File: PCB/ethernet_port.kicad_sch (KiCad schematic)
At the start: 53 parts, among them IC10 MMBT3904-AQ, IC11 MMBT3904-AQ, IC5 W5500, IC6 CP2102N-A02-GQFN24, IC7 USBLC6-2SC6, J1 USB_C_Receptacle_USB2.0_16P, J2 TMJ0026ABNL, Y3 ASE-25.000MHZ-LC-T

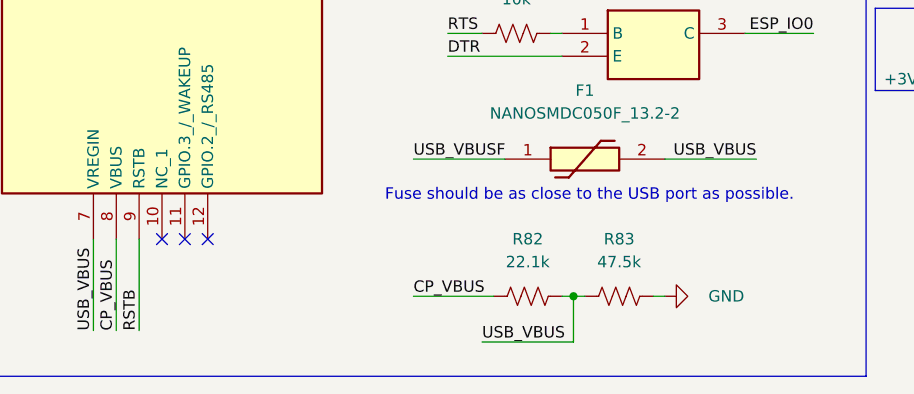
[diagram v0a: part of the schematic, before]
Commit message: Add bottom hand-solder caps and update BOM
Update PCB to add bottom-side hand-solder 0805 capacitor footprints and sync BOM. DarkMagic.csv: increment 0.1uF part count (34→35) and 4.7uF count (1→2) and update component lists. DarkMagic.kicad_pcb: add two B.Cu hand-solder capacitor footprints (C7, C10), adjust several footprint attributes (mark many SMD/TH pads as DNP or set solder_mask_margin), tweak some pad/part positions and UUIDs, and rename one net from /USB_VBUS to /CP_VBUS. Also add generated files (PCB/bom/ibom.html and PCB/database/project.db) and other production file updates to keep project metadata in sync.
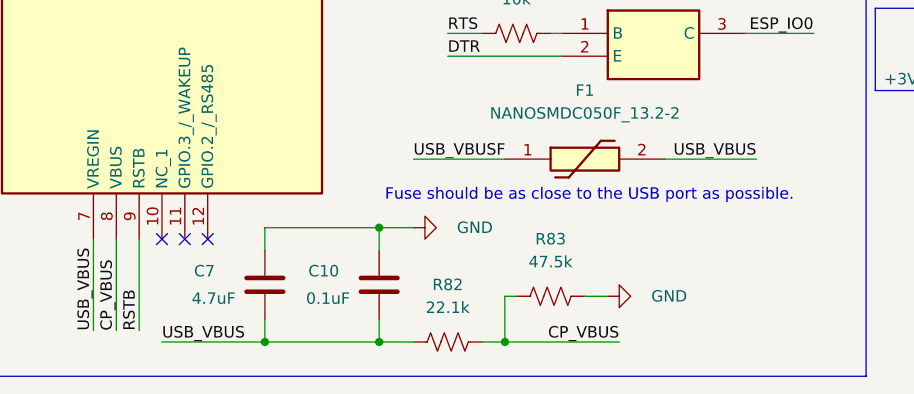
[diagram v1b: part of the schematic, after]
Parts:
- added C10: 0.1uF, Capacitor_SMD:C_0805_2012Metric_Pad1.18x1.45mm_HandSolder, symbol Device:C
- added C7: 4.7uF, Capacitor_SMD:C_0805_2012Metric_Pad1.18x1.45mm_HandSolder, symbol Device:C
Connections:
- net CP_VBUS: now also R83.1
- net GND: now also C10.2, C7.2
- net USB_VBUS: now also C10.1, C7.1; no longer R83.1
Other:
- moved on the sheet: R82, R83

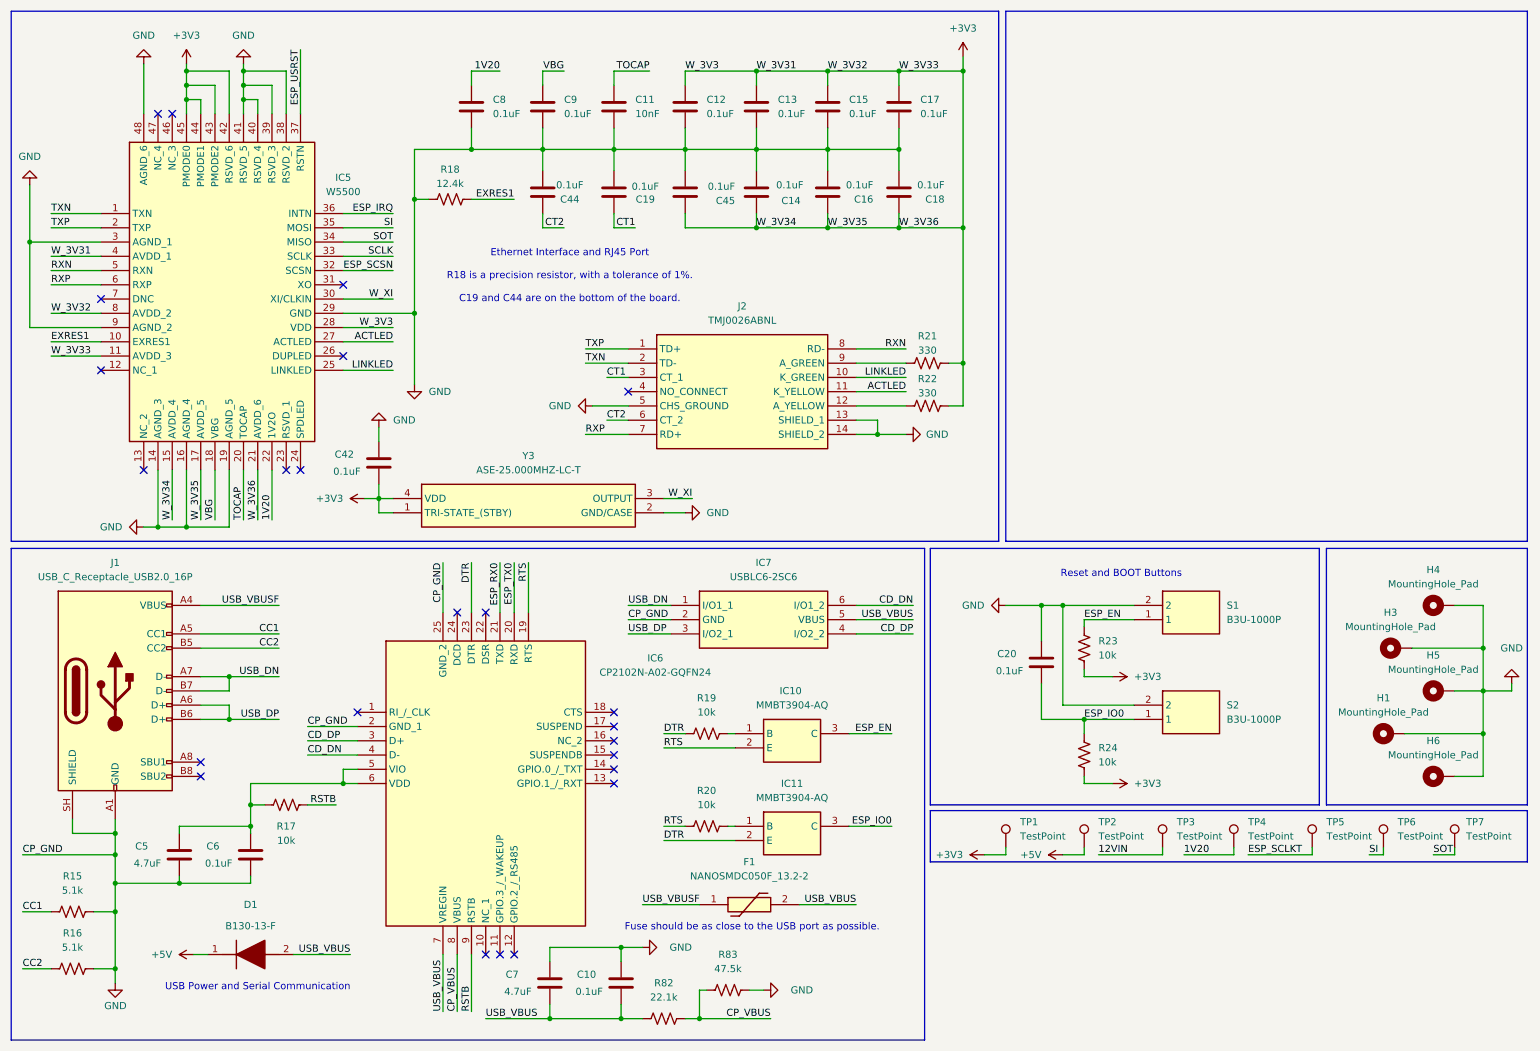
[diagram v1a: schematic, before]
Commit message: Add four 49.9Ω resistors and update PCB
Add R89–R92 as 49.9Ω SMD 0805 hand-solder footprints and corresponding BOM entries. Update PCB layout with new footprints, vias and copper segments to connect the parts into +3V3 and related signal nets (RX/TX pairs), adjust silk/fab properties, and tweak trace geometry. Update production files (BOM, designators, positions, netlist, production archive) and ethernet_port schematic to reflect the changes; add KiCad schematic lock file.
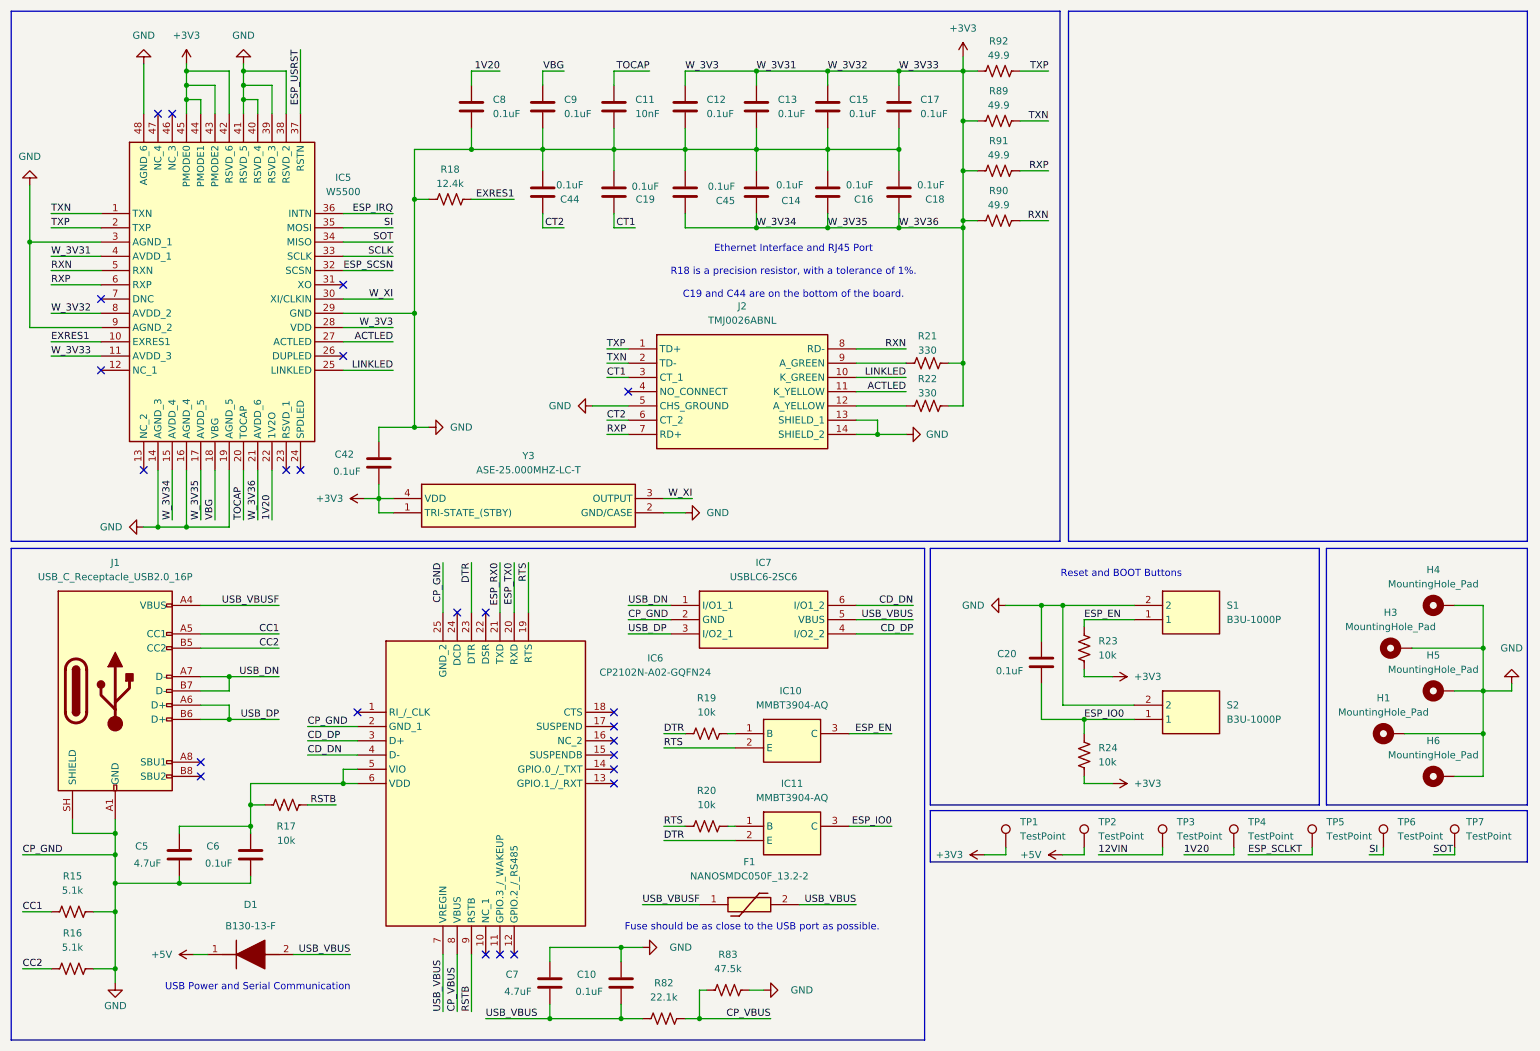
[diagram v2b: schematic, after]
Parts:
- added R89, R90, R91, R92: 49.9, Resistor_SMD:R_0805_2012Metric_Pad1.20x1.40mm_HandSolder, symbol Device:R_US
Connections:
- net +3V3: now also R89.1, R90.1, R91.1, R92.1
- net RXN: now also R90.2
- net RXP: now also R91.2
- net TXN: now also R89.2
- net TXP: now also R92.2

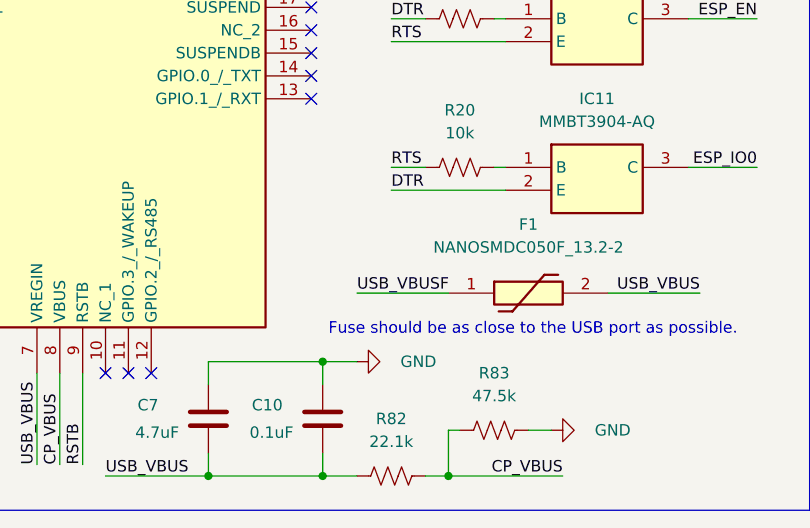
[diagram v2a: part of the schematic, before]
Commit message: PCB: Reroute nets and update component value
Modify DarkMagic.kicad_pcb to correct power routing and update a component value. Changes include: changed a component Value from "CDCLVC1106PWR" to "5PB1106PGGI8", reassigned a pad/net from GND to +3V3, moved a via, removed and added several F.Cu segments (cleaned up GND segments and added +3V3 traces), and adjusted a board polygon/outline coordinate. These edits fix net connections and reflect the correct part designation in the PCB layout.
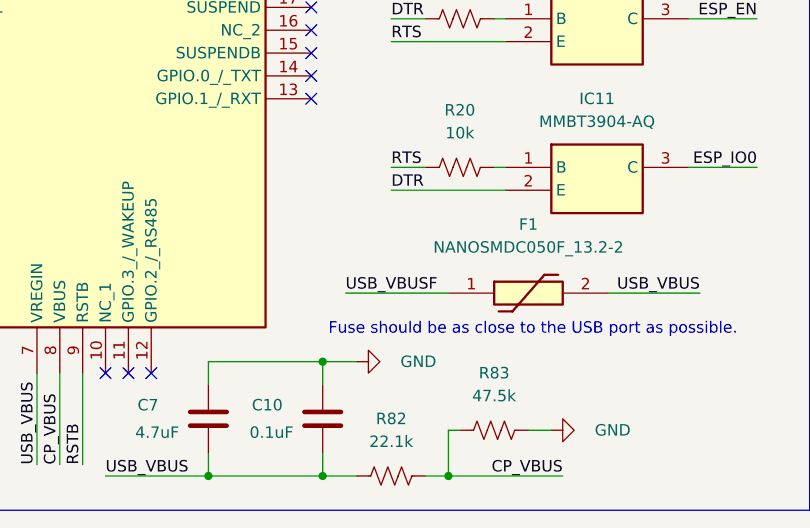
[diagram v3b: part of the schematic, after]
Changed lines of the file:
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@@
 	(wire
 		(pts
-			(xy 125.73 172.72) (xy 135.89 172.72)
+			(xy 124.46 172.72) (xy 135.89 172.72)
 		)
 		(stroke
@@
 	)
 	(label "USB_VBUSF"
-		(at 125.73 172.72 0)
-		(effects
-			(font
+		(at 124.46 172.72 0)
+		(effects
+			(font

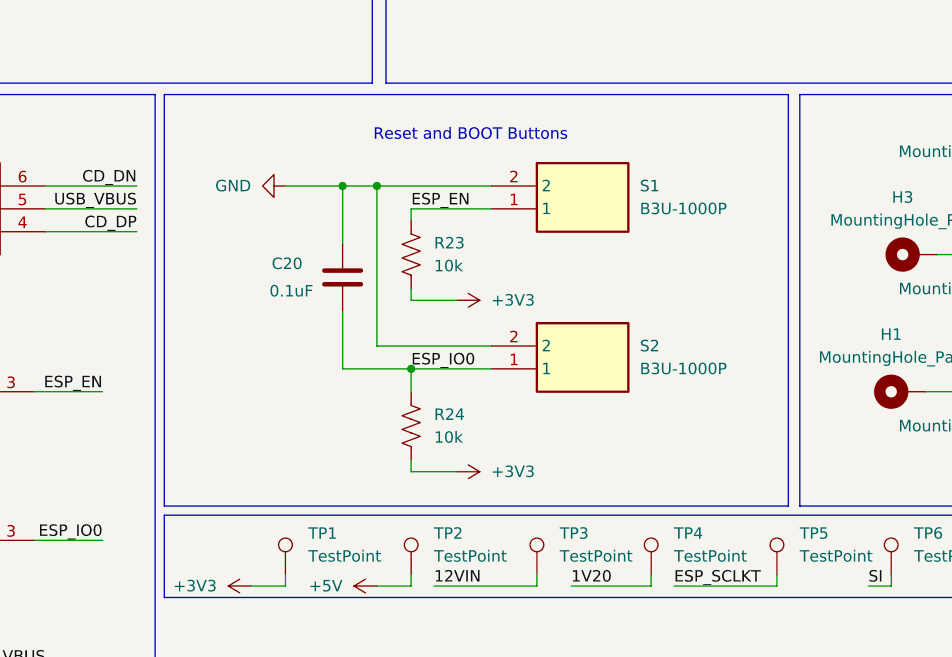
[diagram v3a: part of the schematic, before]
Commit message: V2 Polishing
Minor layout optimizations, including removed vias and rerouted power rails
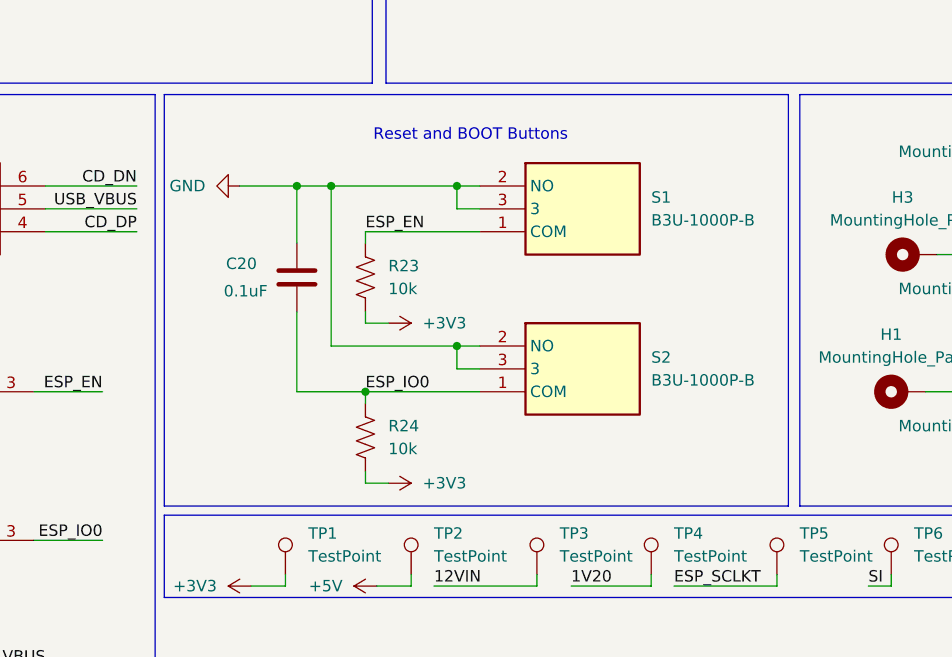
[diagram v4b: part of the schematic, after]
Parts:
- removed S1, S2: B3U-1000P, DarkMagic:B3U-1000P, symbol B3U-1000P:B3U-1000P
- added S1: B3U-1000P-B, DarkMagic:B3U1000PB, symbol B3U-1000P-B:B3U-1000P-B
- added S2: B3U-1000P-B, B3U1000PB, symbol B3U-1000P-B:B3U-1000P-B
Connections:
- net ESP_EN: now also S1.1 (COM)
- net ESP_IO0: now also S2.1 (COM)
- net GND: now also S1.2 (NO), S1.3, S2.2 (NO), S2.3
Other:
- moved on the sheet: C20, R23, R24

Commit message: feat: initialize project with ESP32 schematic, ethernet port layout, and base firmware.
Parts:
- added TP8: TestPoint, TestPoint:TestPoint_Pad_D3.0mm, symbol Connector:TestPoint
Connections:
- net USB_VBUS: now also TP8.1
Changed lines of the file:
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@@
 	(text "USB Power and Serial Communication"
 		(exclude_from_sim no)
-		(at 57.15 187.452 0)
+		(at 57.15 193.294 0)
 		(effects
 			(font
@@
 		(color 0 0 0 0)
 	)
+	(junction
+		(at 66.04 181.61)
+		(diameter 0)
+		(color 0 0 0 0)
+	)
 	(no_connect
 		(at 120.65 148.59)
@@
 	(wire
 		(pts
+			(xy 69.85 186.69) (xy 66.04 186.69)
+		)
+		(stroke
+			(width 0)
+			(type default)
+		)
+	)
+	(wire
+		(pts
 			(xy 158.75 49.53) (xy 158.75 52.07)
 		)
@@
 	(wire
 		(pts
+			(xy 66.04 181.61) (xy 78.74 181.61)
+		)
+		(stroke
+			(width 0)
+			(type default)
+		)
+	)
+	(wire
+		(pts
 			(xy 78.74 87.63) (xy 78.74 90.17)
 		)
@@
 	(wire
 		(pts
-			(xy 63.5 181.61) (xy 73.66 181.61)
+			(xy 63.5 181.61) (xy 66.04 181.61)
 		)
 		(stroke
@@
 	(wire
 		(pts
+			(xy 66.04 186.69) (xy 66.04 181.61)
+		)
+		(stroke
+			(width 0)
+			(type default)
+		)
+	)
+	(wire
+		(pts
 			(xy 146.05 24.13) (xy 146.05 26.67)
 		)
@@
 	)
 	(label "USB_VBUS"
-		(at 73.66 181.61 180)
+		(at 78.74 181.61 180)
 		(effects
 			(font
@@
 					(unit 1)
 				)
+			)
+		)
+	)
+	(symbol
+		(lib_id "Connector:TestPoint")
+		(at 69.85 186.69 270)
+		(unit 1)
+		(body_style 1)
+		(exclude_from_sim no)
+		(in_bom no)
+		(on_board yes)
+		(in_pos_files yes)
+		(dnp no)
+		(fields_autoplaced yes)
+		(property "Reference" "TP8"
+			(at 74.93 185.4199 90)
+			(show_name no)
+			(do_not_autoplace no)
+			(effects
+				(font
+					(size 1.27 1.27)
+				)
+				(justify left)
+			)
+		)
+		(property "Value" "TestPoint"
+			(at 74.93 187.9599 90)
+			(show_name no)
+			(do_not_autoplace no)
+			(effects
+				(font
+					(size 1.27 1.27)
+				)
+				(justify left)
+			)
+		)
+		(property "Footprint" "TestPoint:TestPoint_Pad_D3.0mm"
+			(at 69.85 191.77 0)
+			(hide yes)
+			(show_name no)
+			(do_not_autoplace no)
+			(effects
+				(font
+					(size 1.27 1.27)
+				)
+			)
+		)
+		(property "Datasheet" ""
+			(at 69.85 191.77 0)
+			(hide yes)
+			(show_name no)
+			(do_not_autoplace no)
+			(effects
+				(font
+					(size 1.27 1.27)
+				)
+			)
+		)
+		(property "Description" "test point"
+			(at 69.85 186.69 0)
+			(hide yes)
+			(show_name no)
+			(do_not_autoplace no)
+			(effects
+				(font
+					(size 1.27 1.27)
+				)
+			)
+		)
+		(property "Maunfacturer Part Number" ""
+			(at 69.85 186.69 0)
+			(hide yes)
+			(show_name no)
+			(do_not_autoplace no)
+			(effects
+				(font
+					(size 1.27 1.27)
+				)
+			)
+		)
+		(property "AVAILABILITY" ""
+			(at 69.85 186.69 0)
+			(hide yes)
+			(show_name no)
+			(do_not_autoplace no)
+			(effects
+				(font
+					(size 1.27 1.27)
+				)
+			)
+		)
+		(property "Check_prices" ""
+			(at 69.85 186.69 0)
+			(hide yes)
+			(show_name no)
+			(do_not_autoplace no)
+			(effects
+				(font
+					(size 1.27 1.27)
+				)
+			)
+		)
+		(property "MF" ""
+			(at 69.85 186.69 0)
+			(hide yes)
+			(show_name no)
+			(do_not_autoplace no)
+			(effects
+				(font
+					(size 1.27 1.27)
+				)
+			)
+		)
+		(property "MP" ""
+			(at 69.85 186.69 0)
+			(hide yes)
+			(show_name no)
+			(do_not_autoplace no)
+			(effects
+				(font
+					(size 1.27 1.27)
+				)
+			)
+		)
+		(property "Maunfacturer_Part_Number" ""
+			(at 69.85 186.69 0)
+			(hide yes)
+			(show_name no)
+			(do_not_autoplace no)
+			(effects
+				(font
+					(size 1.27 1.27)
+				)
+			)
+		)
+		(property "PACKAGE" ""
+			(at 69.85 186.69 0)
+			(hide yes)
+			(show_name no)
+			(do_not_autoplace no)
+			(effects
+				(font
+					(size 1.27 1.27)
+				)
+			)
+		)
+		(property "PARTREV" ""
+			(at 69.85 186.69 0)
+			(hide yes)
+			(show_name no)
+			(do_not_autoplace no)
+			(effects
+				(font
+					(size 1.27 1.27)
+				)
+			)
+		)
+		(property "PRICE" ""
+			(at 69.85 186.69 0)
+			(hide yes)
+			(show_name no)
+			(do_not_autoplace no)
+			(effects
+				(font
+					(size 1.27 1.27)
+				)
+			)
+		)
+		(property "STANDARD" ""
+			(at 69.85 186.69 0)
+			(hide yes)
+			(show_name no)
+			(do_not_autoplace no)
+			(effects
+				(font
+					(size 1.27 1.27)
+				)
+			)
+		)
+		(property "SnapEDA_Link" ""
+			(at 69.85 186.69 0)
+			(hide yes)
+			(show_name no)
+			(do_not_autoplace no)
+			(effects
+				(font
+					(size 1.27 1.27)
+				)
+			)
+		)
+		(pin "1"
+		)
+		(instances
+			(project "DarkMagic"
+				(path "/a56e5a4d-a458-4415-ac98-e2a94f5ef798"
+					(reference "TP8")
+					(unit 1)
+				)
